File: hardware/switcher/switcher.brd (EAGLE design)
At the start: 55 x 82 mm, 9 parts, among them IC1 L293E

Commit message: finish boards
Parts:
- removed J3, J4: (no value), SparkFun-Connectors:1X03
- removed J5: (no value), SparkFun-Connectors:1X04
- added BLUE, RED, WHITE, YELLOW: (no value), SparkFun-Connectors:1X01
- added GND, VCC: (no value), SparkFun-Connectors:1X03
- moved J1 42.7 mm to (29.2, 63.5), turned to 270 degrees
- moved J2 35.6 mm to (41.9, 63.5), turned to 270 degrees
- moved C2 12.0 mm to (7.62, 6.35)
- moved C1 11.9 mm to (17.8, 6.35)
- moved IC1 9.74 mm to (12.7, 52.1)
- moved IC2 9.61 mm to (12.7, 19.1)
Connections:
- removed net P2.4: IC1.15
- new net P2.5: IC1.15, J1.3
- net GND: now also GND.1, GND.2, GND.3
- net MOTOR-BLUE: now also BLUE.1
- net MOTOR-RED: now also RED.1
- net MOTOR-WHITE: now also WHITE.1
- net MOTOR-YELLOW: now also YELLOW.1
- net P3.4: now also J1.10
- net P3.5: now also J1.11
- net P3.6: now also J1.12
- net VCC: now also VCC.1, VCC.2, VCC.3
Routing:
- net GND: track 0.00 -> 132.9 mm
- net N$6: track 116.0 -> 0.00 mm, vias 3 -> 0
- net N$16: track 98.6 -> 0.00 mm, vias 2 -> 0
- net VCC: track 0.00 -> 93.1 mm
- net N$14: track 91.7 -> 0.00 mm, vias 1 -> 0
- net N$11: track 77.0 -> 0.00 mm, vias 1 -> 0
- net N$7: track 66.6 -> 0.00 mm
- net N$13: track 51.7 -> 0.00 mm, vias 1 -> 0
- net 9V: track 0.00 -> 48.4 mm
- net N$3: track 47.7 -> 0.00 mm, vias 1 -> 0
- net MOTOR-BLUE: track 0.00 -> 36.0 mm
- net MOTOR-WHITE: track 0.00 -> 31.7 mm
- net P3.4: track 0.00 -> 31.1 mm, vias 0 -> 1
- net N$10: track 30.9 -> 0.00 mm
- net N$15: track 29.7 -> 0.00 mm
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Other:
- board size 55 x 82 mm -> 50 x 80 mm
- board text added: "Switcher Board Derailleurs"
- board text removed: "+"
- board text removed: "-"
- board text removed: "1.4"
- board text removed: "1.5"
- board text removed: "3.5"
- board text removed: "4.3"
- board text removed: "Alice Stevens"
- board text removed: "BLUE"
- board text removed: "Deraileurs"
- board text removed: "Motor Module"
- board text removed: "RED"
- board text removed: "V1.1"
- board text removed: "WHITE"
- board text removed: "YELLOW"

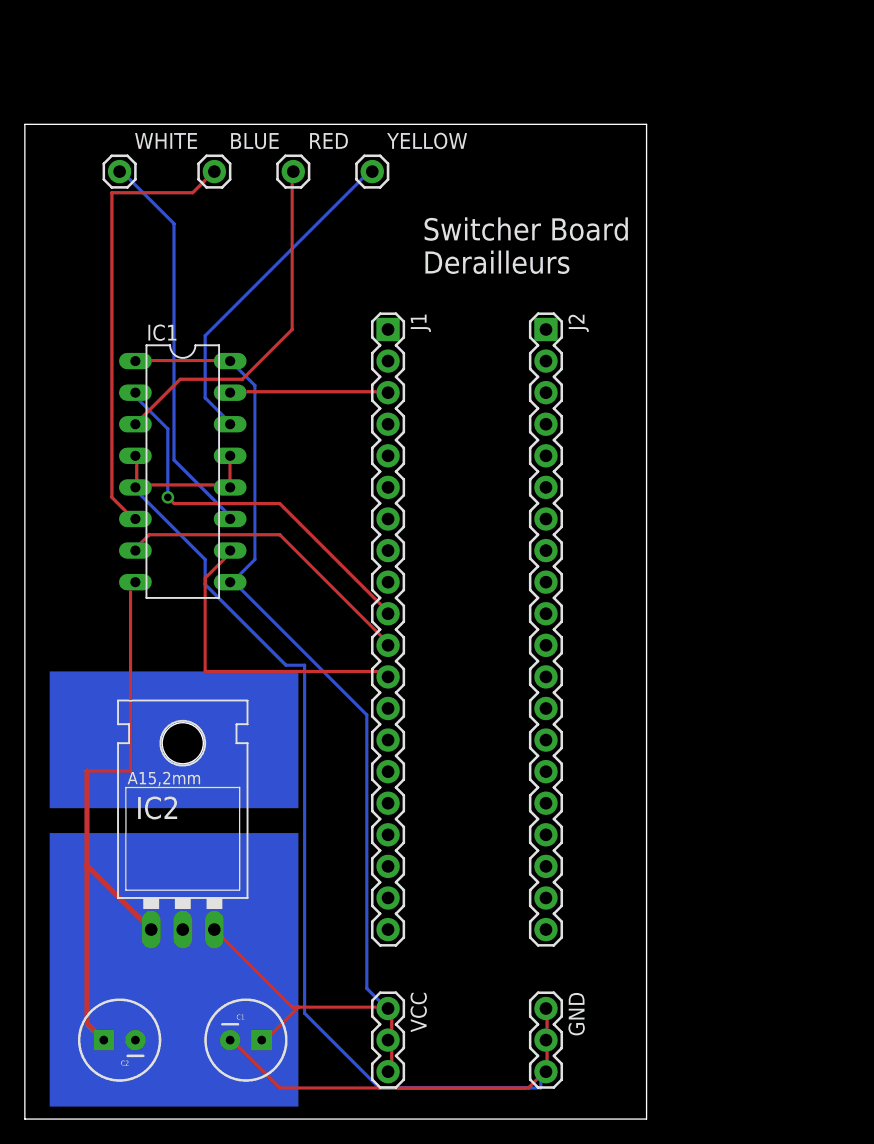
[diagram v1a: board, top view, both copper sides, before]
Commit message: Finish routing all boards, schematics are consitant, and all deliverable requirements are met..
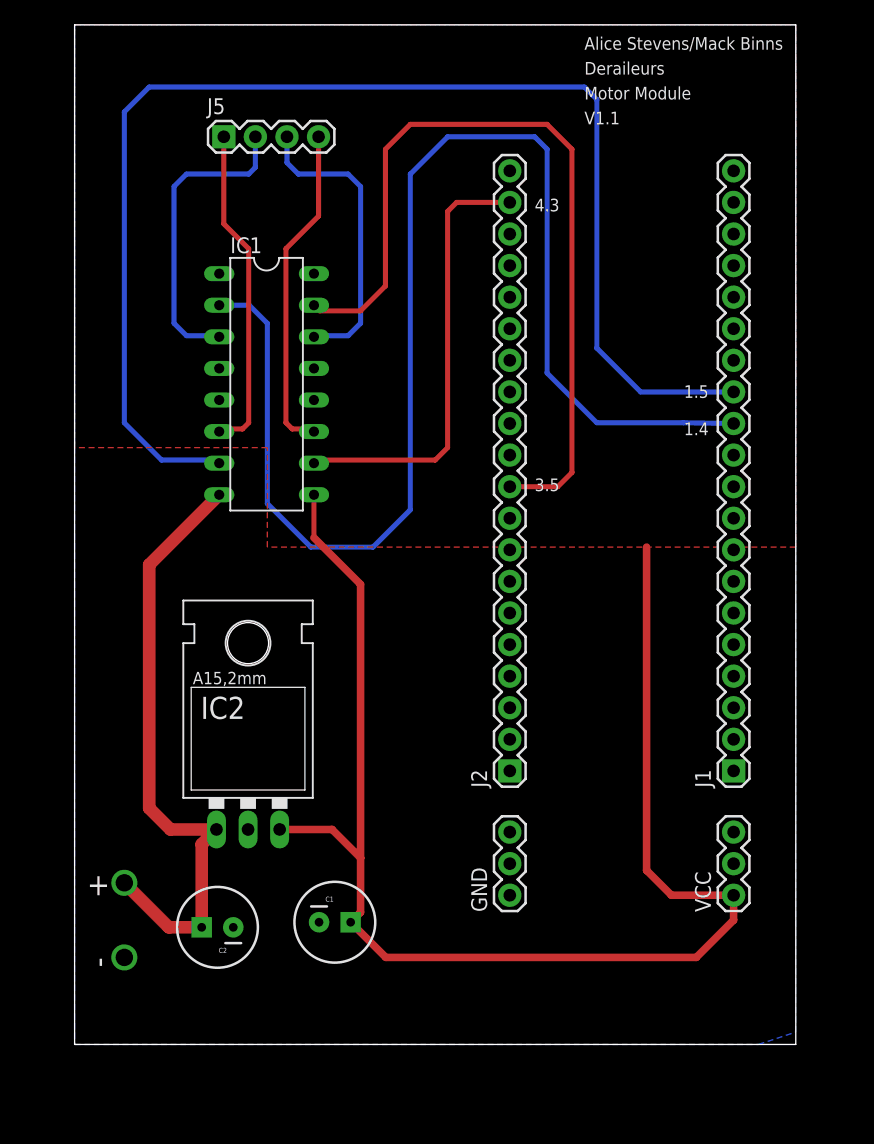
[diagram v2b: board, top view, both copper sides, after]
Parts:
- removed BLUE, RED, WHITE, YELLOW: (no value), SparkFun-Connectors:1X01
- added J5: 9v, SparkFun-Connectors:1X04
- GND: value (none) -> 0v
- J1, J2: value (none) -> 3.3v
- VCC: value (none) -> 5v
- moved J1 45.1 mm to (57.0, 28.0), turned to 90 degrees
- moved J2 35.6 mm to (39.0, 28.0), turned to 90 degrees
- moved VCC 29.2 mm to (57.0, 18.0), turned to 90 degrees
- moved C2 12.0 mm to (15.5, 15.4)
- moved C1 11.9 mm to (24.9, 15.8)
- moved IC1 9.74 mm to (19.4, 59.1)
- moved IC2 9.61 mm to (17.9, 27.1)
- moved GND 9.56 mm to (39.0, 18.0), turned to 90 degrees
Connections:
- removed net P2.5: IC1.15, J1.3
- removed net P3.4: IC1.2, J1.10
- removed net P3.6: IC1.10, J1.12
- new net P1.4: IC1.2, J1.12
- new net P1.5: IC1.7, J1.13
- new net P4.3: IC1.10, J2.19
- net GND: no longer GND.2, GND.3
- net MOTOR-BLUE: now also J5.1; no longer BLUE.1
- net MOTOR-RED: now also J5.2; no longer RED.1
- net MOTOR-WHITE: now also J5.4; no longer WHITE.1
- net MOTOR-YELLOW: now also J5.3; no longer YELLOW.1
- net P3.5: now also IC1.15, J2.10; no longer IC1.7, J1.11
- net VCC: no longer VCC.2, VCC.3
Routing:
- net GND: track 132.9 -> 0.00 mm, vias 0 -> 1
- net P1.4: track 0.00 -> 107.5 mm
- net P1.5: track 0.00 -> 105.7 mm
- net P3.5: track 24.7 -> 65.9 mm
- net P4.3: track 0.00 -> 35.6 mm
- net P3.4: track 31.1 -> 0.00 mm, vias 1 -> 0
- net P3.6: track 25.5 -> 0.00 mm
- net VCC: track 93.1 -> 112.8 mm
- net P2.5: track 12.7 -> 0.00 mm
- net MOTOR-BLUE: track 36.0 -> 26.5 mm
- net MOTOR-WHITE: track 31.7 -> 26.6 mm
- net MOTOR-RED: track 28.5 -> 24.7 mm
- net MOTOR-YELLOW: track 26.8 -> 24.0 mm
- net 9V: track 48.4 -> 49.7 mm, vias 0 -> 1
- added copper zone on layer 16, net GND
- added copper zone on layer 1, net VCC
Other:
- board size 50 x 80 mm -> 58 x 82 mm
- board text added: "+"
- board text added: "-"
- board text added: "1.4"
- board text added: "1.5"
- board text added: "3.5"
- board text added: "4.3"
- board text added: "Alice Stevens/Mack Binns"
- board text added: "BLUE"
- board text added: "Deraileurs"
- board text added: "Motor Module"
- board text added: "RED"
- board text added: "V1.1"
- board text added: "WHITE"
- board text added: "YELLOW"
- board text removed: "Switcher Board Derailleurs"
